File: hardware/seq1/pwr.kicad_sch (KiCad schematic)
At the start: 4 parts, among them J3 Conn_02x08_Odd_Even, U7 TLV1117-33

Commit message: schematic and layout for v1 board
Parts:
- added C16: 47u, Capacitor_THT:CP_Radial_D5.0mm_P2.50mm, symbol Device:C_Polarized_US
- added D10: SB160, Diode_THT:D_DO-41_SOD81_P10.16mm_Horizontal, symbol Diode:SB160
- added D9: SB160, Diode_THT:D_DO-41_SOD81_P2.54mm_Vertical_AnodeUp, symbol Diode:SB160
- C15: value 10n -> 100n
- U7: footprint (none) -> Package_TO_SOT_SMD:SOT-223-3_TabPin2
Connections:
- net +12V: now also D10.1 (K); no longer J3.10 (Pin_10), J3.9 (Pin_9)
- net +3V3_A: now also C16.1
- net -12V: now also D9.2 (A); no longer J3.1 (Pin_1), J3.2 (Pin_2)
- net GND: now also C16.2
- net CV renamed CV_O
- net GATE renamed GATE_O
- new net: D9.1 (K), J3.1 (Pin_1), J3.2 (Pin_2)
- new net: D10.2 (A), J3.10 (Pin_10), J3.9 (Pin_9)

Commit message: layout clean up
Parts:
- added H1, H2: MountingHole, MountingHole:MountingHole_3.5mm, symbol Mechanical:MountingHole
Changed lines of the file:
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@@
+	)
+	(symbol
+		(lib_id "Mechanical:MountingHole")
+		(at 101.6 139.7 0)
+		(unit 1)
+		(exclude_from_sim no)
+		(in_bom yes)
+		(on_board yes)
+		(dnp no)
+		(fields_autoplaced yes)
+		(property "Reference" "H1"
+			(at 104.14 138.4299 0)
+			(effects
+				(font
+					(size 1.27 1.27)
+				)
+				(justify left)
+			)
+		)
+		(property "Value" "MountingHole"
+			(at 104.14 140.9699 0)
+			(effects
+				(font
+					(size 1.27 1.27)
+				)
+				(justify left)
+			)
+		)
+		(property "Footprint" "MountingHole:MountingHole_3.5mm"
+			(at 101.6 139.7 0)
+			(effects
+				(font
+					(size 1.27 1.27)
+				)
+				(hide yes)
+			)
+		)
+		(property "Datasheet" "~"
+			(at 101.6 139.7 0)
+			(effects
+				(font
+					(size 1.27 1.27)
+				)
+				(hide yes)
+			)
+		)
+		(property "Description" "Mounting Hole without connection"
+			(at 101.6 139.7 0)
+			(effects
+				(font
+					(size 1.27 1.27)
+				)
+				(hide yes)
+			)
+		)
+		(instances
+			(project "seq1"
+				(path "/8ddbd4cb-c9ed-4e84-b41b-81a0645f4a34/ad5d672c-4b33-4fb3-a40b-97941b1249c6"
+					(reference "H1")
+					(unit 1)
+				)
+			)
+		)
 	)
 	(symbol
@@
 					(unit 1)
 				)
+			)
+		)
+	)
+	(symbol
+		(lib_id "Mechanical:MountingHole")
+		(at 101.6 152.4 0)
+		(unit 1)
+		(exclude_from_sim no)
+		(in_bom yes)
+		(on_board yes)
+		(dnp no)
+		(fields_autoplaced yes)
+		(property "Reference" "H2"
+			(at 104.14 151.1299 0)
+			(effects
+				(font
+					(size 1.27 1.27)
+				)
+				(justify left)
+			)
+		)
+		(property "Value" "MountingHole"
+			(at 104.14 153.6699 0)
+			(effects
+				(font
+					(size 1.27 1.27)
+				)
+				(justify left)
+			)
+		)
+		(property "Footprint" "MountingHole:MountingHole_3.5mm"
+			(at 101.6 152.4 0)
+			(effects
+				(font
+					(size 1.27 1.27)
+				)
+				(hide yes)
+			)
+		)
+		(property "Datasheet" "~"
+			(at 101.6 152.4 0)
+			(effects
+				(font
+					(size 1.27 1.27)
+				)
+				(hide yes)
+			)
+		)
+		(property "Description" "Mounting Hole without connection"
+			(at 101.6 152.4 0)
+			(effects
+				(font
+					(size 1.27 1.27)
+				)
+				(hide yes)
+			)
+		)
+		(instances
+			(project "seq1"
+				(path "/8ddbd4cb-c9ed-4e84-b41b-81a0645f4a34/ad5d672c-4b33-4fb3-a40b-97941b1249c6"
+					(reference "H2")
+					(unit 1)
+				)

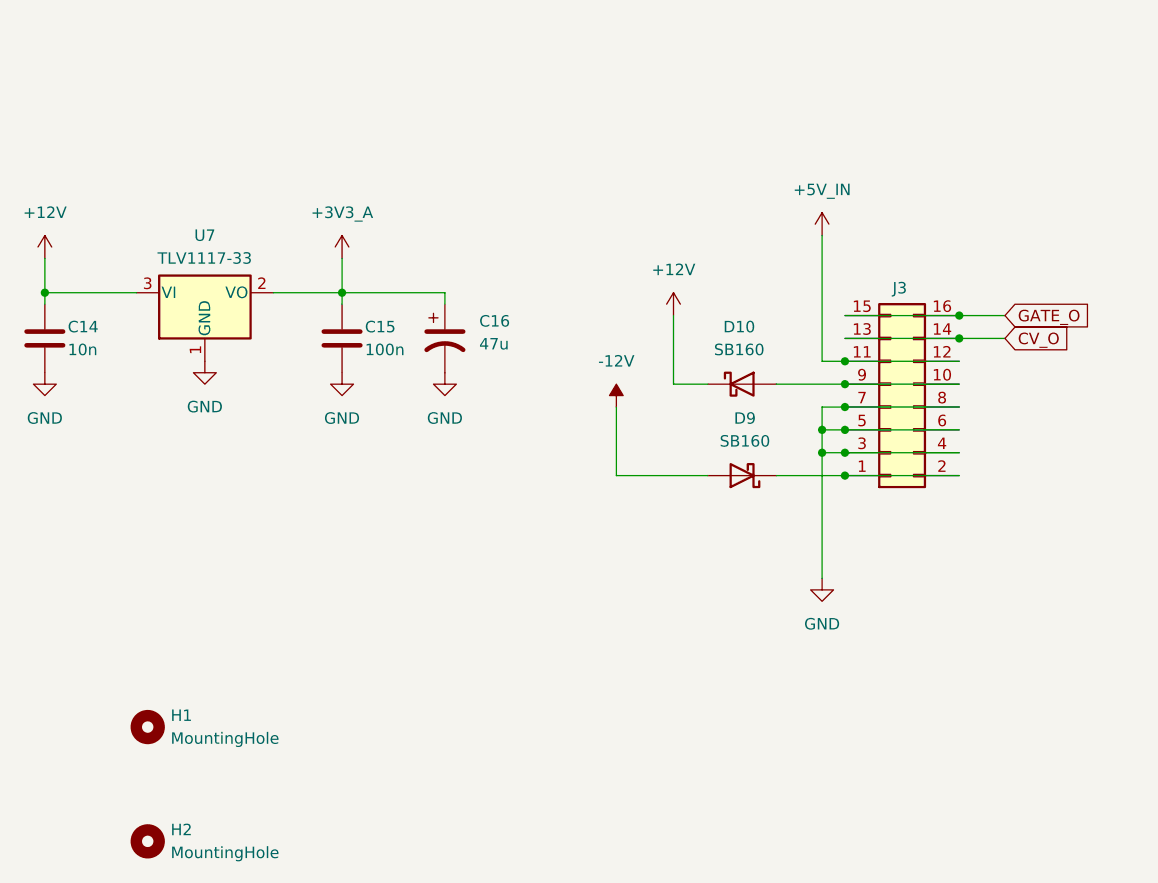
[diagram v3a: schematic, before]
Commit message: updating the board with new line in
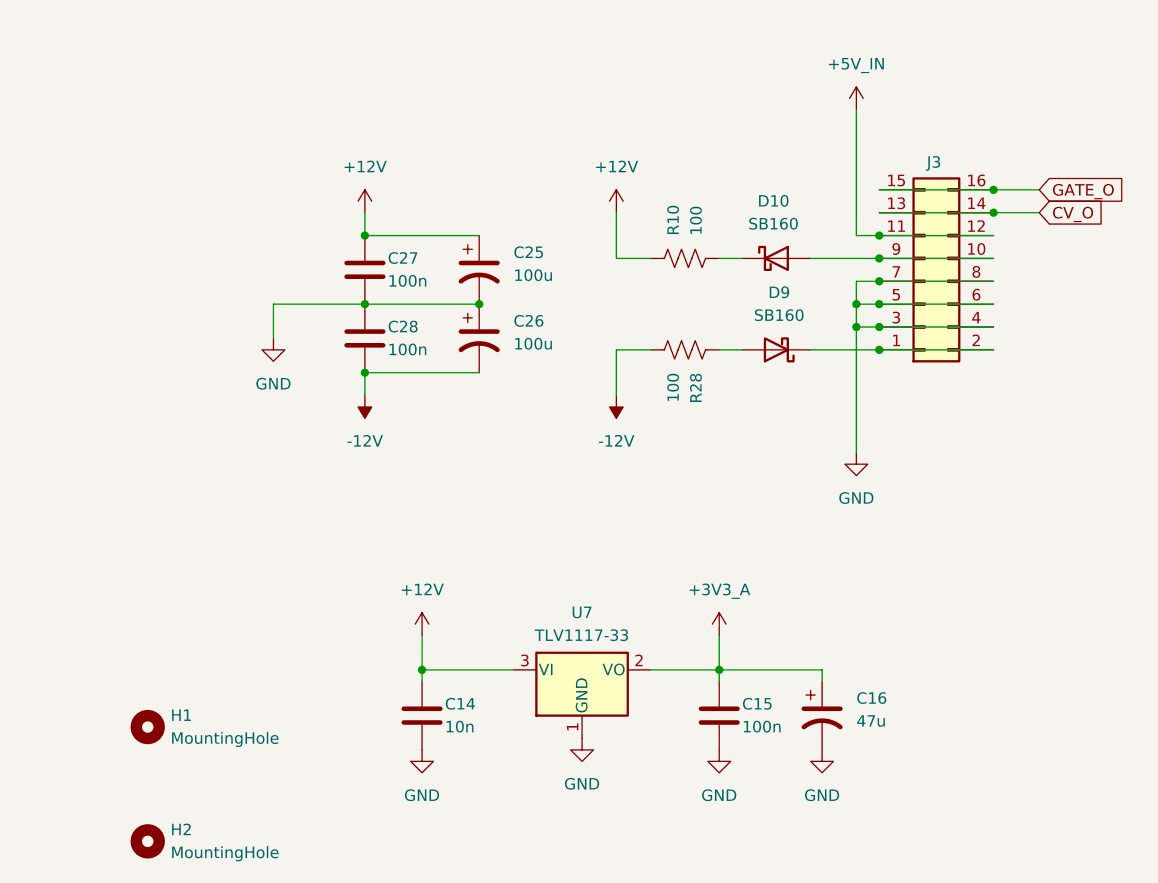
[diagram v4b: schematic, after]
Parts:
- added C25, C26: 100u, Capacitor_THT:CP_Radial_D6.3mm_P2.50mm, symbol Device:C_Polarized_US
- added C27, C28: 100n, Capacitor_THT:C_Disc_D5.0mm_W2.5mm_P2.50mm, symbol Device:C
- added R10: 100, Resistor_THT:R_Axial_DIN0204_L3.6mm_D1.6mm_P2.54mm_Vertical, symbol Device:R_US
- added R28: 100, Resistor_THT:R_Axial_DIN0207_L6.3mm_D2.5mm_P7.62mm_Horizontal, symbol Device:R_US
- C14, C15: footprint Capacitor_THT:C_Disc_D5.0mm_W2.5mm_P5.00mm -> Capacitor_THT:C_Disc_D5.0mm_W2.5mm_P2.50mm
- D10: footprint Diode_THT:D_DO-41_SOD81_P10.16mm_Horizontal -> Diode_THT:D_DO-41_SOD81_P2.54mm_Vertical_KathodeUp
- H1, H2: footprint MountingHole:MountingHole_3.5mm -> MountingHole:MountingHole_3.2mm_M3_DIN965
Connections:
- net +12V: now also C25.1, C27.1, R10.1; no longer D10.1 (K)
- net -12V: now also C26.2, C28.2, R28.2; no longer D9.2 (A)
- net GND: now also C25.2, C26.1, C27.2, C28.1
- new net: D10.1 (K), R10.2
- new net: D9.2 (A), R28.1
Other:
- company: (none) -> idyllm
- title: (none) -> Sequencer
- moved on the sheet: C14, C15, C16, D10, D9, J3, U7

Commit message: layout for v2 board (WIP) with risers part of same schematic/PBC
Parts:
- D10: footprint Diode_THT:D_DO-41_SOD81_P2.54mm_Vertical_KathodeUp -> Diode_THT:D_DO-35_SOD27_P2.54mm_Vertical_AnodeUp
- D9: footprint Diode_THT:D_DO-41_SOD81_P2.54mm_Vertical_AnodeUp -> Diode_THT:D_DO-35_SOD27_P2.54mm_Vertical_AnodeUp
- R10, R28: value 100 -> 10
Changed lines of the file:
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@@
 (kicad_sch
-	(version 20231120)
+	(version 20250114)
 	(generator "eeschema")
-	(generator_version "8.0")
+	(generator_version "9.0")
 	(paper "A4")
 	(title_block
@@
 			)
 		)
-		(property "Footprint" "Diode_THT:D_DO-41_SOD81_P2.54mm_Vertical_KathodeUp"
+		(property "Footprint" "Diode_THT:D_DO-35_SOD27_P2.54mm_Vertical_AnodeUp"
 			(at 171.45 92.075 0)
 			(effects
@@
 			)
 		)
-		(property "Value" "100"
+		(property "Value" "10"
 			(at 160.0201 100.33 0)
 			(effects
@@
 			)
 		)
-		(property "Footprint" "Diode_THT:D_DO-41_SOD81_P2.54mm_Vertical_AnodeUp"
+		(property "Footprint" "Diode_THT:D_DO-35_SOD27_P2.54mm_Vertical_AnodeUp"
 			(at 171.45 93.345 0)
 			(effects
@@
 			)
 		)
-		(property "Value" "100"
+		(property "Value" "10"
 			(at 162.5599 85.09 0)
 			(effects

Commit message: updated schematic title blocks for v2, generated gerbers
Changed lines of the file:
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@@
 	(title_block
 		(title "Sequencer")
-		(date "2024-10-14")
-		(rev "1.1")
+		(date "2025-11-07")
+		(rev "2.0")
 		(company "idyllm")
 		(comment 1 "CC BY-SA 4.0")
@@
 	)
 	(junction
+		(at 138.43 85.09)
+		(diameter 0)
+		(color 0 0 0 0)
+	)
+	(junction
 		(at 182.88 95.25)
+		(diameter 0)
+		(color 0 0 0 0)
+	)
+	(junction
+		(at 138.43 100.33)
 		(diameter 0)
 		(color 0 0 0 0)
@@
 	)
 	(junction
+		(at 176.53 133.35)
+		(diameter 0)
+		(color 0 0 0 0)
+	)
+	(junction
 		(at 180.34 92.71)
 		(diameter 0)
@@
 	(wire
 		(pts
+			(xy 180.34 71.12) (xy 180.34 85.09)
+		)
+		(stroke
+			(width 0)
+			(type default)
+		)
+	)
+	(wire
+		(pts
 			(xy 182.88 97.79) (xy 175.26 97.79)
 		)
@@
 	(wire
 		(pts
-			(xy 165.1 129.54) (xy 165.1 133.35)
+			(xy 176.53 129.54) (xy 176.53 133.35)
 		)
 		(stroke
@@
 	(wire
 		(pts
+			(xy 165.1 133.35) (xy 176.53 133.35)
+		)
+		(stroke
+			(width 0)
+			(type default)
+		)
+	)
+	(wire
+		(pts
 			(xy 182.88 92.71) (xy 195.58 92.71)
 		)
@@
 	(wire
 		(pts
-			(xy 176.53 133.35) (xy 165.1 133.35)
-		)
-		(stroke
-			(width 0)
-			(type default)
-		)
-	)
-	(wire
-		(pts
 			(xy 180.34 95.25) (xy 180.34 92.71)
 		)
@@
 		(pts
 			(xy 182.88 82.55) (xy 195.58 82.55)
-		)
-		(stroke
-			(width 0)
-			(type default)
-		)
-	)
-	(wire
-		(pts
-			(xy 180.34 71.12) (xy 180.34 85.09)
 		)
 		(stroke
@@
 	(symbol
 		(lib_id "power:+5V")
-		(at 165.1 129.54 0)
+		(at 176.53 129.54 0)
 		(unit 1)
 		(exclude_from_sim no)
@@
 		(fields_autoplaced yes)
 		(property "Reference" "#PWR054"
-			(at 165.1 133.35 0)
+			(at 176.53 133.35 0)
 			(effects
 				(font
@@
 		)
 		(property "Value" "+3V3_A"
-			(at 165.1 124.46 0)
+			(at 176.53 124.46 0)
 			(effects
 				(font
@@
 		)
 		(property "Footprint" ""
-			(at 165.1 129.54 0)
+			(at 176.53 129.54 0)
 			(effects
 				(font
@@
 		)
 		(property "Datasheet" ""
-			(at 165.1 129.54 0)
+			(at 176.53 129.54 0)
 			(effects
 				(font
@@
 		)
 		(property "Description" "Power symbol creates a global label with name \"+5V\""
-			(at 165.1 129.54 0)
+			(at 176.53 129.54 0)
 			(effects
 				(font
@@
 	)
 	(symbol
+		(lib_id "power:PWR_FLAG")
+		(at 138.43 100.33 0)
+		(mirror x)
+		(unit 1)
+		(exclude_from_sim no)
+		(in_bom yes)
+		(on_board yes)
+		(dnp no)
+		(fields_autoplaced yes)
+		(property "Reference" "#FLG03"
+			(at 138.43 102.235 0)
+			(effects
+				(font
+					(size 1.27 1.27)
+				)
+				(hide yes)
+			)
+		)
+		(property "Value" "PWR_FLAG"
+			(at 138.43 105.41 0)
+			(effects
+				(font
+					(size 1.27 1.27)
+				)
+			)
+		)
+		(property "Footprint" ""
+			(at 138.43 100.33 0)
+			(effects
+				(font
+					(size 1.27 1.27)
+				)
+				(hide yes)
+			)
+		)
+		(property "Datasheet" "~"
+			(at 138.43 100.33 0)
+			(effects
+				(font
+					(size 1.27 1.27)
+				)
+				(hide yes)
+			)
+		)
+		(property "Description" "Special symbol for telling ERC where power comes from"
+			(at 138.43 100.33 0)
+			(effects
+				(font
+					(size 1.27 1.27)
+				)
+				(hide yes)
+			)
+		)
+		(pin "1"
+		)
+		(instances
+			(project ""
+				(path "/8ddbd4cb-c9ed-4e84-b41b-81a0645f4a34/ad5d672c-4b33-4fb3-a40b-97941b1249c6"
+					(reference "#FLG03")
+					(unit 1)
+				)
+			)
+		)
+	)
+	(symbol
 		(lib_id "power:+12V")
 		(at 132.08 129.54 0)
@@
 					(unit 1)
 				)
+			)
+		)
+	)
+	(symbol
+		(lib_id "power:PWR_FLAG")
+		(at 138.43 85.09 0)
+		(unit 1)
+		(exclude_from_sim no)
+		(in_bom yes)
+		(on_board yes)
+		(dnp no)
+		(fields_autoplaced yes)
+		(property "Reference" "#FLG02"
+			(at 138.43 83.185 0)
+			(effects
+				(font
+					(size 1.27 1.27)
+				)
+				(hide yes)
+			)
+		)
+		(property "Value" "PWR_FLAG"
+			(at 138.43 80.01 0)
+			(effects
+				(font
+					(size 1.27 1.27)
+				)
+			)
+		)
+		(property "Footprint" ""
+			(at 138.43 85.09 0)
+			(effects
+				(font
+					(size 1.27 1.27)
+				)
+				(hide yes)
+			)
+		)
+		(property "Datasheet" "~"
+			(at 138.43 85.09 0)
+			(effects
+				(font
+					(size 1.27 1.27)
+				)
+				(hide yes)
+			)
+		)
+		(property "Description" "Special symbol for telling ERC where power comes from"
+			(at 138.43 85.09 0)
+			(effects
+				(font
+					(size 1.27 1.27)
+				)
+				(hide yes)
+			)
+		)
+		(pin "1"
+		)
+		(instances
+			(project ""
+				(path "/8ddbd4cb-c9ed-4e84-b41b-81a0645f4a34/ad5d672c-4b33-4fb3-a40b-97941b1249c6"
+					(reference "#FLG02")
+					(unit 1)
+				)
